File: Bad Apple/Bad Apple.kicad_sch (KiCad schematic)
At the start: 0 parts

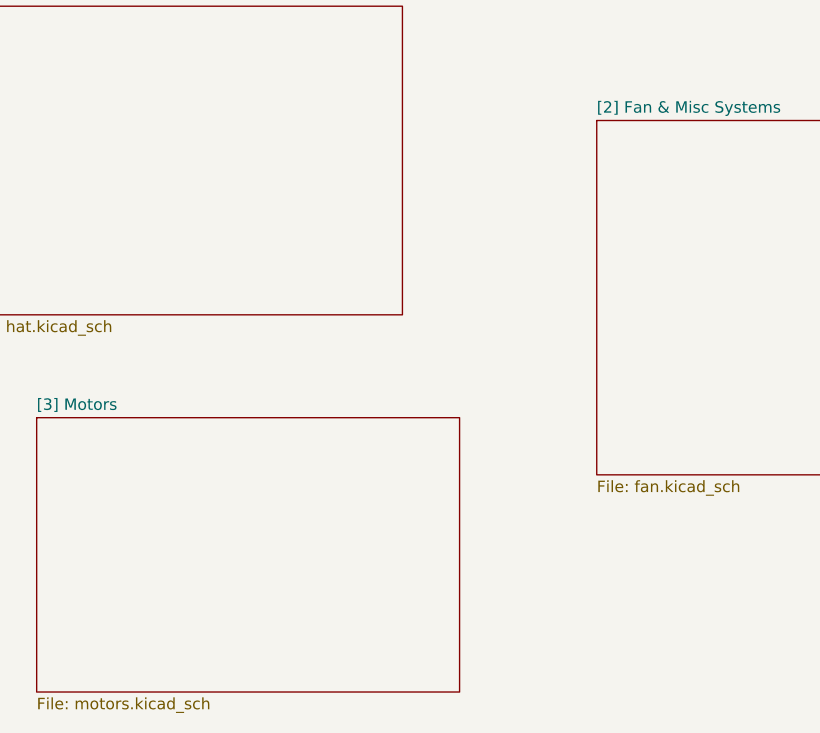
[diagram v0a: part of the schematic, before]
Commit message: feat(pcb): motor subsystem
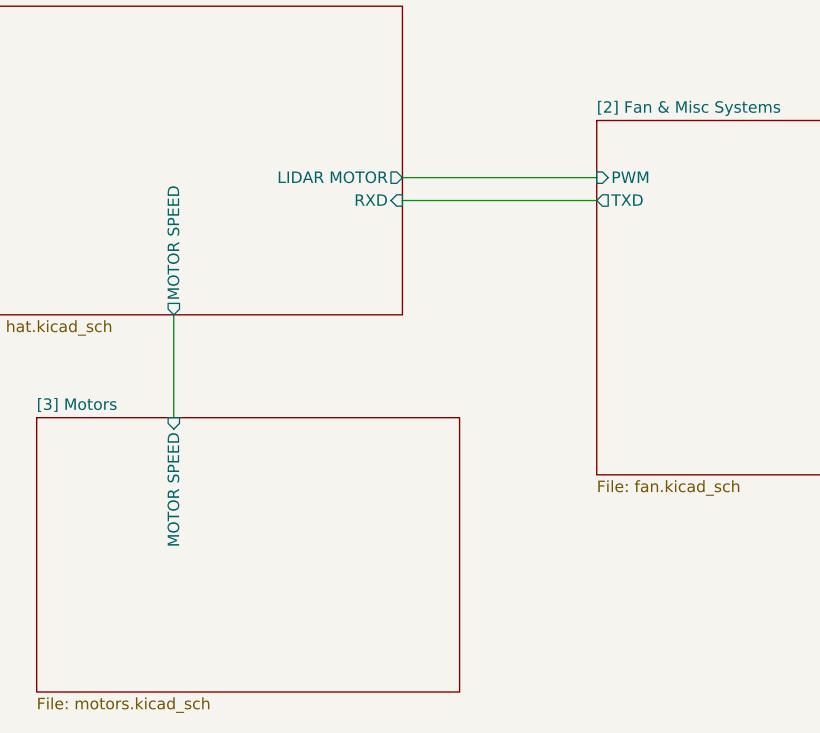
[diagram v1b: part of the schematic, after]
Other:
- sheet [1] HAT Interface ports: added LIDAR MOTOR, MOTOR SPEED, RXD; removed none
- sheet [2] Fan & Misc Systems ports: added PWM, TXD; removed none
- sheet [3] Motors ports: added MOTOR SPEED; removed none
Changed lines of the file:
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@@
 		(comment 4 "Schematic Overview")
+	)
+	(wire
+		(pts
+			(xy 80.01 52.07) (xy 101.6 52.07)
+		)
+		(stroke
+			(width 0)
+			(type default)
+		)
+	)
+	(wire
+		(pts
+			(xy 80.01 49.53) (xy 101.6 49.53)
+		)
+		(stroke
+			(width 0)
+			(type default)
+		)
+	)
+	(wire
+		(pts
+			(xy 54.61 64.77) (xy 54.61 76.2)
+		)
+		(stroke
+			(width 0)
+			(type default)
+		)
 	)
 	(sheet
@@
 				)
 				(justify left top)
+			)
+		)
+		(pin "LIDAR MOTOR" output
+			(at 80.01 49.53 0)
+			(effects
+				(font
+					(size 1.27 1.27)
+				)
+				(justify right)
+			)
+		)
+		(pin "RXD" input
+			(at 80.01 52.07 0)
+			(effects
+				(font
+					(size 1.27 1.27)
+				)
+				(justify right)
+			)
+		)
+		(pin "MOTOR SPEED" output
+			(at 54.61 64.77 270)
+			(effects
+				(font
+					(size 1.27 1.27)
+				)
+				(justify left)
 			)
 		)
@@
 			)
 		)
+		(pin "PWM" input
+			(at 101.6 49.53 180)
+			(effects
+				(font
+					(size 1.27 1.27)
+				)
+				(justify left)
+			)
+		)
+		(pin "TXD" output
+			(at 101.6 52.07 180)
+			(effects
+				(font
+					(size 1.27 1.27)
+				)
+				(justify left)
+			)
+		)
 		(instances
 			(project "Bad Apple"
@@
 			)
 		)
+		(pin "MOTOR SPEED" input
+			(at 54.61 76.2 90)
+			(effects
+				(font
+					(size 1.27 1.27)
+				)
+				(justify right)
+			)
+		)

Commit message: feat(pcb): connections n stuff
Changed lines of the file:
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@@
+	(wire
+		(pts
+			(xy 50.8 64.77) (xy 50.8 77.47)
+		)
+		(stroke
+			(width 0)
+			(type default)
+		)
+	)
 	(wire
 		(pts
@@
 		(pts
 			(xy 80.01 49.53) (xy 101.6 49.53)
-		)
-		(stroke
-			(width 0)
-			(type default)
-		)
-	)
-	(wire
-		(pts
-			(xy 54.61 64.77) (xy 54.61 76.2)
 		)
 		(stroke
@@
 		)
 		(pin "MOTOR SPEED" output
-			(at 54.61 64.77 270)
+			(at 50.8 64.77 270)
 			(effects
 				(font
@@
 	)
 	(sheet
-		(at 39.37 76.2)
+		(at 33.02 77.47)
 		(size 46.99 30.48)
 		(exclude_from_sim no)
@@
 		)
 		(property "Sheetname" "[3] Motors"
-			(at 39.37 75.4884 0)
+			(at 33.02 76.7584 0)
 			(effects
 				(font
@@
 		)
 		(property "Sheetfile" "motors.kicad_sch"
-			(at 39.37 107.2646 0)
+			(at 33.02 108.5346 0)
 			(effects
 				(font
@@
 		)
 		(pin "MOTOR SPEED" input
-			(at 54.61 76.2 90)
+			(at 50.8 77.47 90)
 			(effects
 				(font

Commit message: feat(pcb): i forgor ☠️
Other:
- sheet [2] Fan & Misc Systems ports: added I^{2}C SCL, I^{2}C SDA, U1E, U1T, U2E, U2T, ~{SERVO ENABLE}; removed none
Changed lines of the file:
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@@
+			)
+		)
+		(pin "U1E" output
+			(at 101.6 69.85 180)
+			(effects
+				(font
+					(size 1.27 1.27)
+				)
+				(justify left)
+			)
+		)
+		(pin "U1T" input
+			(at 101.6 72.39 180)
+			(effects
+				(font
+					(size 1.27 1.27)
+				)
+				(justify left)
+			)
+		)
+		(pin "U2E" output
+			(at 101.6 74.93 180)
+			(effects
+				(font
+					(size 1.27 1.27)
+				)
+				(justify left)
+			)
+		)
+		(pin "U2T" input
+			(at 101.6 77.47 180)
+			(effects
+				(font
+					(size 1.27 1.27)
+				)
+				(justify left)
+			)
+		)
+		(pin "~{SERVO ENABLE}" input
+			(at 101.6 57.15 180)
+			(effects
+				(font
+					(size 1.27 1.27)
+				)
+				(justify left)
+			)
+		)
+		(pin "I^{2}C SCL" input
+			(at 101.6 60.96 180)
+			(effects
+				(font
+					(size 1.27 1.27)
+				)
+				(justify left)
+			)
+		)
+		(pin "I^{2}C SDA" bidirectional
+			(at 101.6 63.5 180)
+			(effects
+				(font
+					(size 1.27 1.27)
+				)
+				(justify left)
 			)
 		)

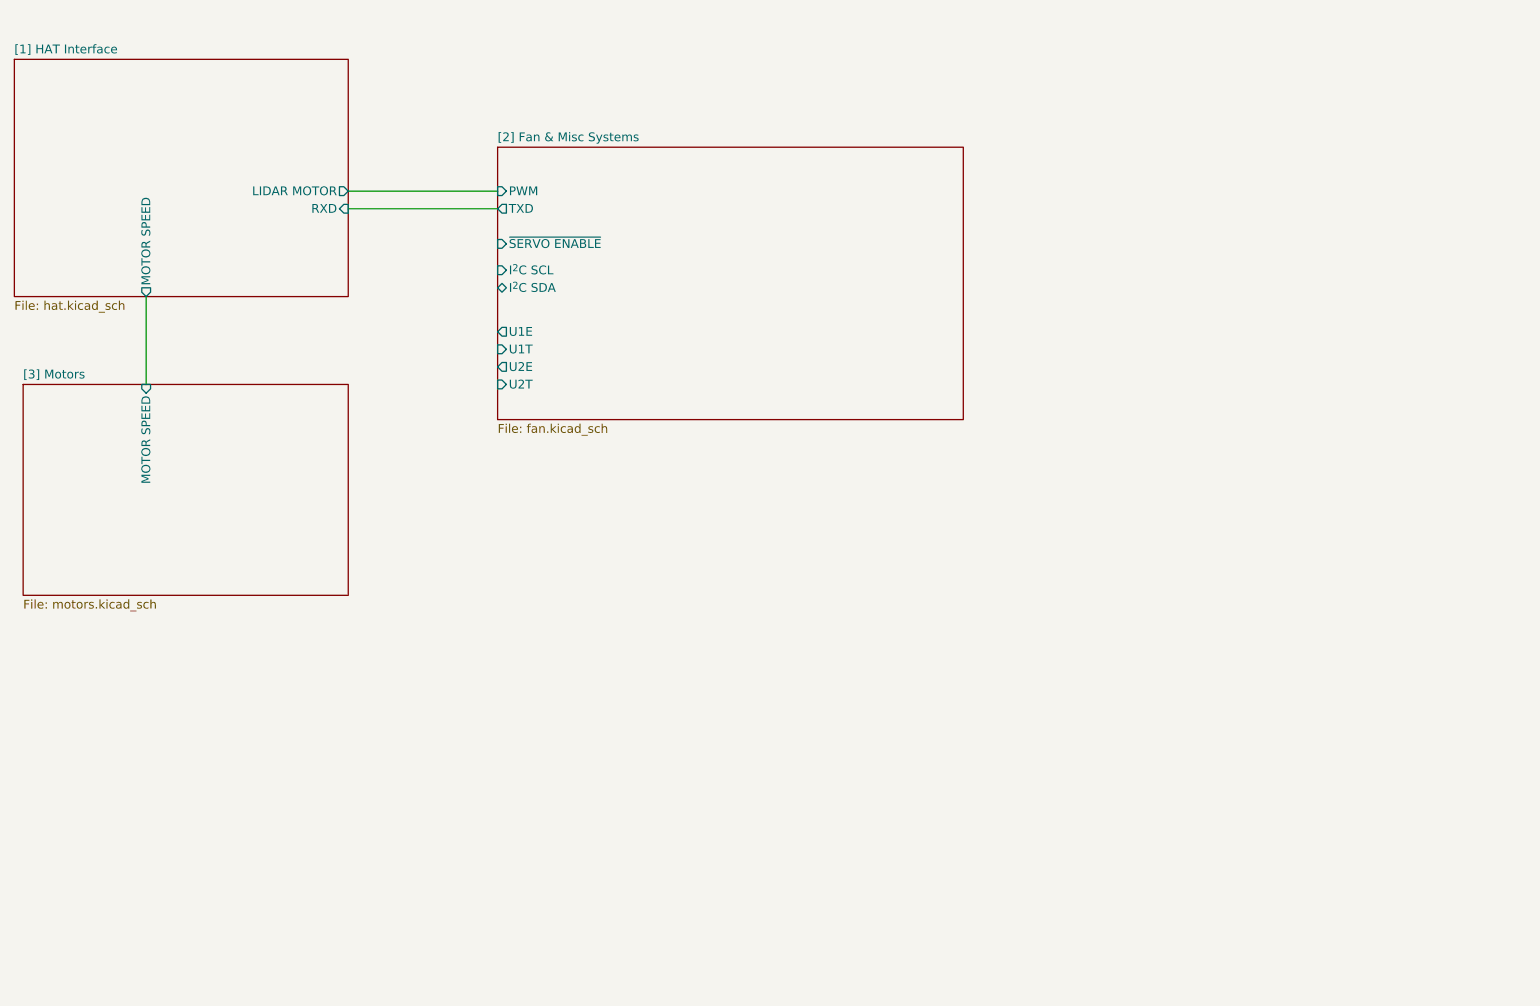
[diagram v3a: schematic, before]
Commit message: chore(pcb): re-structured schematics to follow a importance-based order
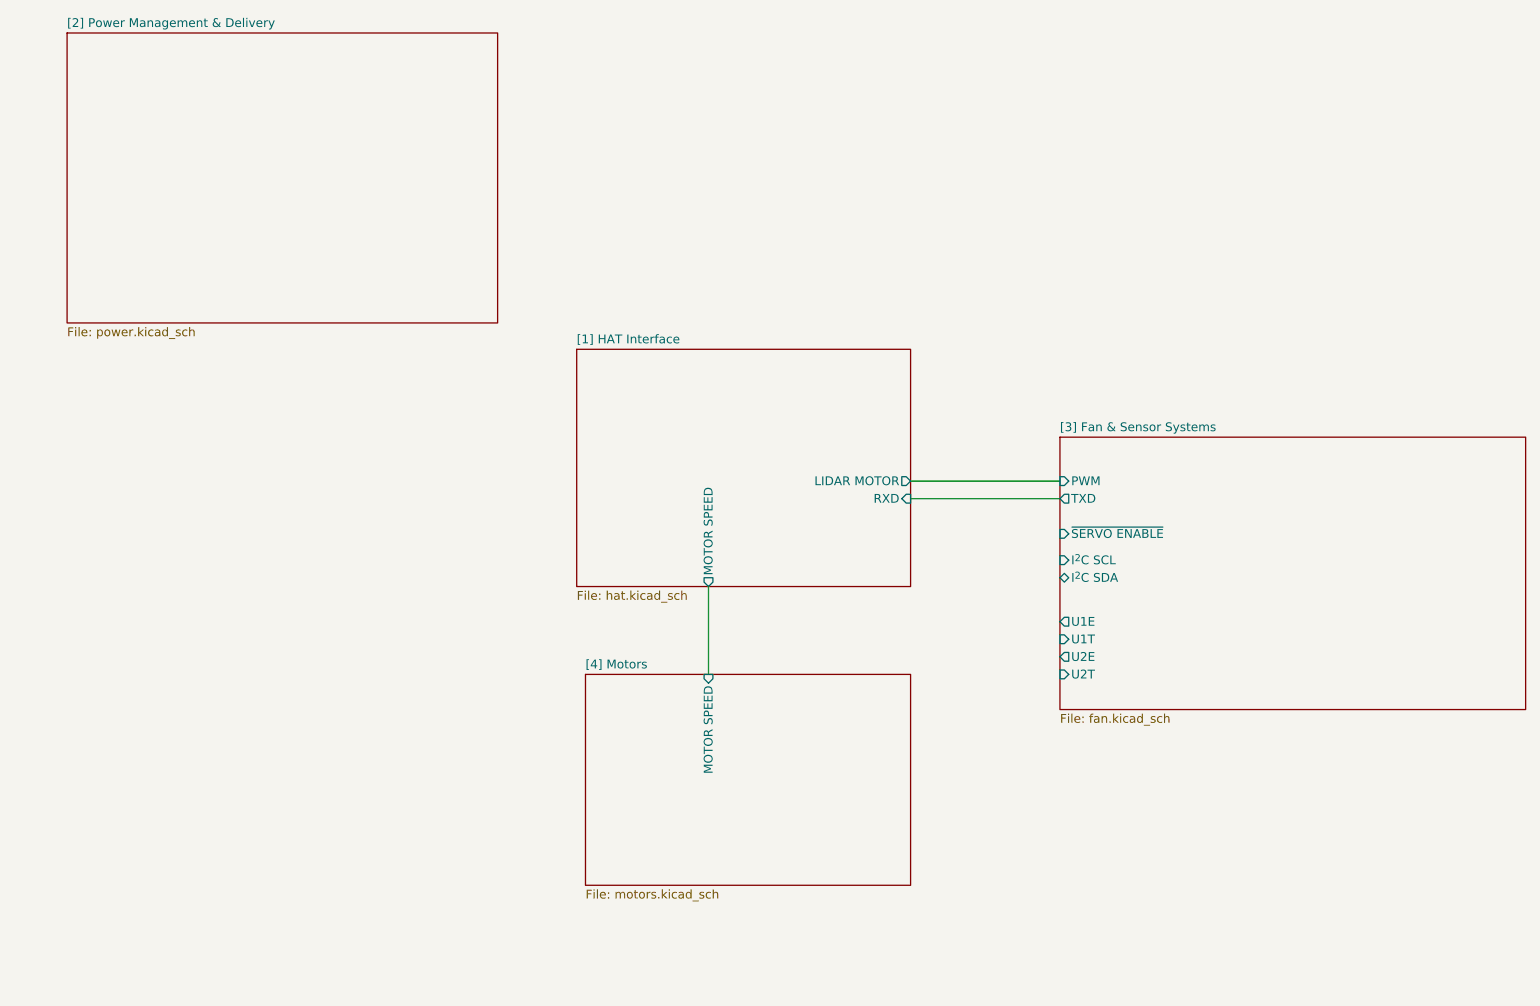
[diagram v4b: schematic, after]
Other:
- sheet [2] Fan & Misc Systems renamed [3] Fan & Sensor Systems
- sheet [3] Motors renamed [4] Motors
- added sheet [2] Power Management & Delivery (power.kicad_sch)
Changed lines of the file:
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@@
 	(wire
 		(pts
-			(xy 50.8 64.77) (xy 50.8 77.47)
+			(xy 132.08 106.68) (xy 132.08 119.38)
 		)
 		(stroke
@@
 	(wire
 		(pts
-			(xy 80.01 52.07) (xy 101.6 52.07)
+			(xy 161.29 93.98) (xy 182.88 93.98)
 		)
 		(stroke
@@
 	(wire
 		(pts
-			(xy 80.01 49.53) (xy 101.6 49.53)
+			(xy 161.29 91.44) (xy 182.88 91.44)
 		)
 		(stroke
@@
 	)
 	(sheet
-		(at 31.75 30.48)
+		(at 39.37 26.67)
+		(size 62.23 41.91)
+		(exclude_from_sim no)
+		(in_bom yes)
+		(on_board yes)
+		(dnp no)
+		(fields_autoplaced yes)
+		(stroke
+			(width 0.1524)
+			(type solid)
+		)
+		(fill
+			(color 0 0 0 0.0000)
+		)
+		(property "Sheetname" "[2] Power Management & Delivery"
+			(at 39.37 25.9584 0)
+			(effects
+				(font
+					(size 1.27 1.27)
+				)
+				(justify left bottom)
+			)
+		)
+		(property "Sheetfile" "power.kicad_sch"
+			(at 39.37 69.1646 0)
+			(effects
+				(font
+					(size 1.27 1.27)
+				)
+				(justify left top)
+			)
+		)
+		(instances
+			(project "Bad Apple"
+				(path "/e63e39d7-6ac0-4ffd-8aa3-1841a4541b55"
+					(page "3")
+				)
+			)
+		)
+	)
+	(sheet
+		(at 113.03 72.39)
 		(size 48.26 34.29)
 		(exclude_from_sim no)
@@
 		)
 		(property "Sheetname" "[1] HAT Interface"
-			(at 31.75 29.7684 0)
+			(at 113.03 71.6784 0)
 			(effects
 				(font
@@
 		)
 		(property "Sheetfile" "hat.kicad_sch"
-			(at 31.75 65.3546 0)
+			(at 113.03 107.2646 0)
 			(effects
 				(font
@@
 		)
 		(pin "LIDAR MOTOR" output
-			(at 80.01 49.53 0)
+			(at 161.29 91.44 0)
 			(effects
 				(font
@@
 		)
 		(pin "RXD" input
-			(at 80.01 52.07 0)
+			(at 161.29 93.98 0)
 			(effects
 				(font
@@
 		)
 		(pin "MOTOR SPEED" output
-			(at 50.8 64.77 270)
+			(at 132.08 106.68 270)
 			(effects
 				(font
@@
 	)
 	(sheet
-		(at 101.6 43.18)
+		(at 182.88 85.09)
 		(size 67.31 39.37)
 		(exclude_from_sim no)
@@
 			(color 0 0 0 0.0000)
 		)
-		(property "Sheetname" "[2] Fan & Misc Systems"
-			(at 101.6 42.4684 0)
+		(property "Sheetname" "[3] Fan & Sensor Systems"
+			(at 182.88 84.3784 0)
 			(effects
 				(font
@@
 		)
 		(property "Sheetfile" "fan.kicad_sch"
-			(at 101.6 83.1346 0)
+			(at 182.88 125.0446 0)
 			(effects
 				(font
@@
 		)
 		(pin "PWM" input
-			(at 101.6 49.53 180)
+			(at 182.88 91.44 180)
 			(effects
 				(font
@@
 		)
 		(pin "TXD" output
-			(at 101.6 52.07 180)
+			(at 182.88 93.98 180)
 			(effects
 				(font
@@
 		)
 		(pin "U1E" output
-			(at 101.6 69.85 180)
+			(at 182.88 111.76 180)
 			(effects
 				(font
@@
 		)
 		(pin "U1T" input
-			(at 101.6 72.39 180)
+			(at 182.88 114.3 180)
 			(effects
 				(font
@@
 		)
 		(pin "U2E" output
-			(at 101.6 74.93 180)
+			(at 182.88 116.84 180)
 			(effects
 				(font
@@
 		)
 		(pin "U2T" input
-			(at 101.6 77.47 180)
+			(at 182.88 119.38 180)
 			(effects
 				(font
@@
 		)
 		(pin "~{SERVO ENABLE}" input
-			(at 101.6 57.15 180)
+			(at 182.88 99.06 180)
 			(effects
 				(font
@@
 		)
 		(pin "I^{2}C SCL" input
-			(at 101.6 60.96 180)
+			(at 182.88 102.87 180)
 			(effects
 				(font
@@
 		)
 		(pin "I^{2}C SDA" bidirectional
-			(at 101.6 63.5 180)
+			(at 182.88 105.41 180)
 			(effects
 				(font
@@
 			(project "Bad Apple"
 				(path "/e63e39d7-6ac0-4ffd-8aa3-1841a4541b55"
-					(page "3")
+					(page "6")
 				)
 			)
@@
 	)
 	(sheet
-		(at 33.02 77.47)
+		(at 114.3 119.38)
 		(size 46.99 30.48)
 		(exclude_from_sim no)
@@
 			(color 0 0 0 0.0000)
 		)
-		(property "Sheetname" "[3] Motors"
-			(at 33.02 76.7584 0)
+		(property "Sheetname" "[4] Motors"
+			(at 114.3 118.6684 0)
 			(effects
 				(font
@@
 		)
 		(property "Sheetfile" "motors.kicad_sch"
-			(at 33.02 108.5346 0)
+			(at 114.3 150.4446 0)
 			(effects
 				(font
@@
 		)
 		(pin "MOTOR SPEED" input
-			(at 50.8 77.47 90)
+			(at 132.08 119.38 90)
 			(effects
 				(font
@@
 			(project "Bad Apple"
 				(path "/e63e39d7-6ac0-4ffd-8aa3-1841a4541b55"
-					(page "4")
-				)
-			)
+					(page "7")
+				)
+			)

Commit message: feat(pcb):  connected everything to the HAT doc(pcb):  Added descriptions to the J1 pinout
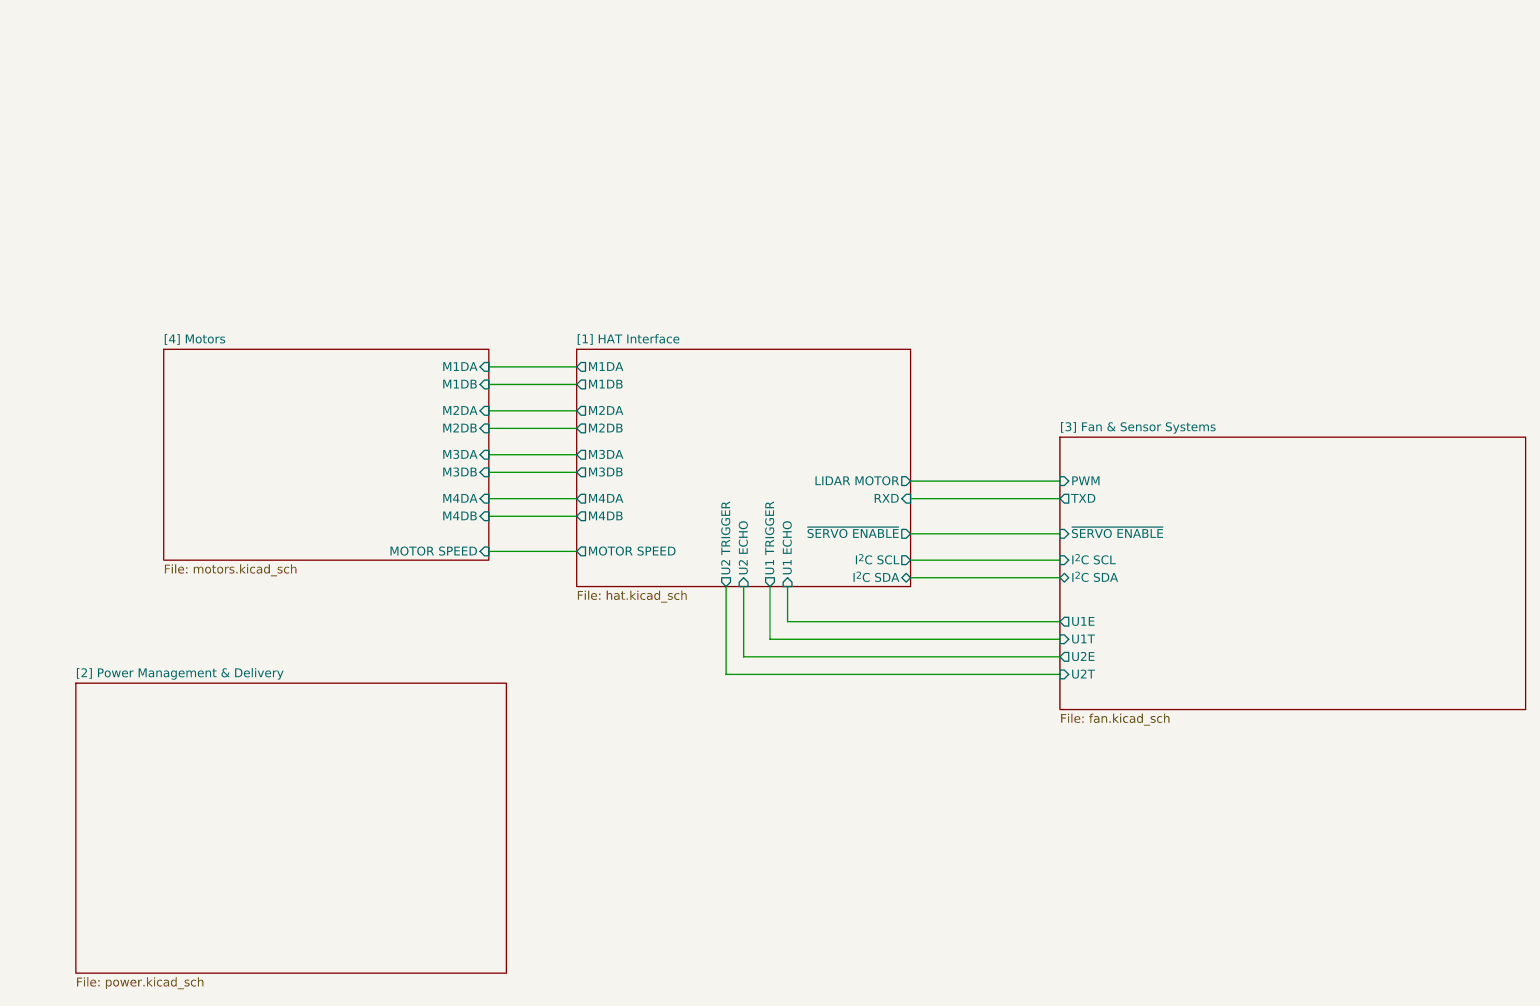
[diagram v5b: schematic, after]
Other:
- sheet [1] HAT Interface ports: added I^{2}C SCL, I^{2}C SDA, M1DA, M1DB, M2DA, M2DB, M3DA, M3DB, M4DA, M4DB, U1 ECHO, U1 TRIGGER, U2 ECHO, U2 TRIGGER, ~{SERVO ENABLE}; removed none
- sheet [4] Motors ports: added M1DA, M1DB, M2DA, M2DB, M3DA, M3DB, M4DA, M4DB; removed none
